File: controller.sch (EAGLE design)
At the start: 70 parts, among them J1 SATA0010225X, J10 ALED_A, J11 ALED_B, J12 ALED_C, J13 FRONT_PANEL, J14 12V, J15 5V, J16 3.3V, J2 USB, J3 ICSP, J4 PUMP, J5 FANS, J6 FLOW, J7 TEMP, J8 TACH_OUT, J9 SHUTDOWN, Q1 NMOSL, Q2 NMOSL, Q3 NMOSL, Q4 NMOSL, Q5 NMOSL, Q6 NMOSL, Q7 NMOSL, Q8 NMOSL, SW1 RESET, U1 PIC32MZ-EF-144, U2 NCP5501DT33, U3 MAX6071A_30, U4 TXU0104, U5 CPC1006N, Y1 24MHz

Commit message: Controller (hopefully) finished
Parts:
- added A1: VXO7805-500, BW-Active:VXO78-500
- added C23, C27: 0.1µF, rcl:C-EUC0603
- added C24: 22µF, rcl:C-EUC0603
- added C25: 10µF, rcl:C-EUC0805
- added C26: 100µF, rcl:CPOL-EUD
- added D1, D2: GS1A-L, BW-Active:DO-214AC-DIODE
- added J17: 12V_WD, pinhead:PINHD-1X2
- added K1: G5Q-1, BW-PassiveMechanical:G5Q-1
- added Q10, Q9: PMOS, BW-Active:SOT23-P-MOSFET
- added Q11: NMOSL, BW-Active:SOT23-N-MOSFET
- added R16, R18: 1kΩ, resistor:R-US_R0603
- added R17: 10kΩ, resistor:R-US_R0603
- added TP1, TP10, TP11, TP12, TP14, TP15, TP2, TP3, TP4, TP5, TP6, TP7, TP8, TP9: RCU-0(J), BW-PassiveMechanical:RCU-0(J)
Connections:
- new net 12V_PUMP: J4.2, K1G$2.P
- new net 12V_PUMP_WD: K1G$2.O, Q10.D
- new net 12V_WD: A1.IN, C25.1, C26.+, Q10.S, Q9.S, R17.2
- new net 12V_WD_PROTECT: Q9.G, R16.1
- new net 12V_WD_RAW: J17.1, Q9.D
- new net 5V_SB: C16.1, C19.1, D1.C, D2.C, J13.1, R12.1, R13.2, R7.2, R8.2, R9.2, TP5.TP, U2.IN, U3.EN, U3.IN
- new net 5V_WD: A1.OUT, C24.1, D2.A, R18.2
- new net PUMP_WD_DRIVE: Q10.G, Q11.D, R17.1
- new net PUMP_WD_RUN: Q11.G, U1.AN36/ETDX1/RJ9
- new net WD_DETECT: R18.1, U1.ERXD0/RH8
- net 12V: now also K1G$1.1, K1G$2.S; no longer J4.2
- net 3.3V: now also C27.1
- net 3V_REF: now also TP6.TP
- net 5V: no longer R12.1, R13.2
- net 5V_USB: now also C23.1, D1.A, TP4.TP; no longer C16.1, C19.1, J13.1, R7.2, R8.2, R9.2, U2.IN, U3.EN, U3.IN
- net ALED_A: now also TP1.TP
- net ALED_B: now also TP2.TP
- net ALED_C: now also TP3.TP
- net ALED_OE: now also TP15.TP
- net FAN_PWM: now also TP14.TP
- net FAN_TACH: now also TP12.TP
- net FLOW_TACH: now also TP8.TP
- net GND: now also A1.GND, C23.2, C24.2, C25.2, C26.-, C27.2, J17.2, K1G$1.2, Q11.S, R16.2
- net PUMP_PWM: now also TP11.TP
- net PUMP_TACH: now also TP10.TP
- net TACH_OUT: now also TP9.TP
- net TEMP_SENSE: now also TP7.TP
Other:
- moved on the sheet: C10, C11, C12, C4, C5, C6, C7, C8, C9, J4, J5, J8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

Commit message: Parts Ordered
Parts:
- R11: value 4.7kΩ -> 2kΩ
- U4: value TXU0104 -> TXU0304-3; device BW-Active:TXU0104 -> BW-Active:TXU0304-3
- U5: value CPC1006N -> CPC1017N; device BW-Active:CPC1006N -> BW-Active:CPC1017N
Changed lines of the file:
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@@
 <part name="C19" library="rcl" library_urn="urn:adsk.eagle:library:334" deviceset="C-EU" device="C0603" package3d_urn="urn:adsk.eagle:package:23616/2" value="0.1µF"/>
 <part name="C20" library="rcl" library_urn="urn:adsk.eagle:library:334" deviceset="C-EU" device="C0603" package3d_urn="urn:adsk.eagle:package:23616/2" value="0.1µF"/>
-<part name="U4" library="BW-Active" library_urn="urn:adsk.eagle:library:33783073" deviceset="TXU0104" device="" package3d_urn="urn:adsk.eagle:package:33783235/2"/>
+<part name="U4" library="BW-Active" library_urn="urn:adsk.eagle:library:33783073" deviceset="TXU0*04" device="-3" package3d_urn="urn:adsk.eagle:package:33783235/2" technology="3"/>
 <part name="R9" library="resistor" library_urn="urn:adsk.eagle:library:348" deviceset="R-US_" device="R0603" package3d_urn="urn:adsk.eagle:package:23555/3" value="100kΩ"/>
 <part name="R8" library="resistor" library_urn="urn:adsk.eagle:library:348" deviceset="R-US_" device="R0603" package3d_urn="urn:adsk.eagle:package:23555/3" value="100kΩ"/>
@@
 <part name="R10" library="resistor" library_urn="urn:adsk.eagle:library:348" deviceset="R-US_" device="R0603" package3d_urn="urn:adsk.eagle:package:23555/3" value="10kΩ"/>
 <part name="Q2" library="BW-Active" library_urn="urn:adsk.eagle:library:33783073" deviceset="SOT23-N-MOSFET" device="" package3d_urn="urn:adsk.eagle:package:33783194/2" value="NMOSL"/>
-<part name="U5" library="BW-Active" library_urn="urn:adsk.eagle:library:33783073" deviceset="CPC1006N" device="" package3d_urn="urn:adsk.eagle:package:33936582/2"/>
-<part name="R11" library="resistor" library_urn="urn:adsk.eagle:library:348" deviceset="R-US_" device="R0603" package3d_urn="urn:adsk.eagle:package:23555/3" value="4.7kΩ"/>
+<part name="U5" library="BW-Active" library_urn="urn:adsk.eagle:library:33783073" deviceset="CPC1017N" device="" package3d_urn="urn:adsk.eagle:package:33936582/3"/>
+<part name="R11" library="resistor" library_urn="urn:adsk.eagle:library:348" deviceset="R-US_" device="R0603" package3d_urn="urn:adsk.eagle:package:23555/3" value="2kΩ"/>
 <part name="Q3" library="BW-Active" library_urn="urn:adsk.eagle:library:33783073" deviceset="SOT23-N-MOSFET" device="" package3d_urn="urn:adsk.eagle:package:33783194/2" value="NMOSL"/>
 <part name="SJ1" library="jumper" library_urn="urn:adsk.eagle:library:252" deviceset="SJ" device="" package3d_urn="urn:adsk.eagle:package:15471/1" value="GNDLINK"/>
@@
 <wire x1="124.46" y1="124.46" x2="127" y2="124.46" width="0.1524" layer="91"/>
 <junction x="127" y="124.46"/>
-</segment>
-<segment>
+<wire x1="127" y1="124.46" x2="129.54" y2="124.46" width="0.1524" layer="91"/>
+<label x="129.54" y="124.46" size="1.778" layer="95"/>
+</segment>
+<segment>

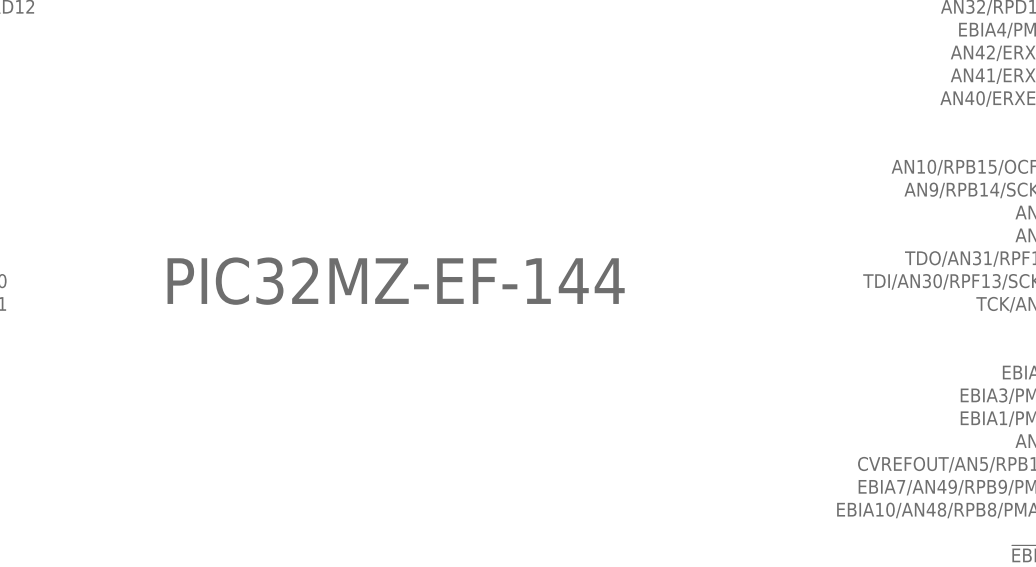
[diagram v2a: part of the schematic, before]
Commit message: Replaced MCU footprint due to earlier error
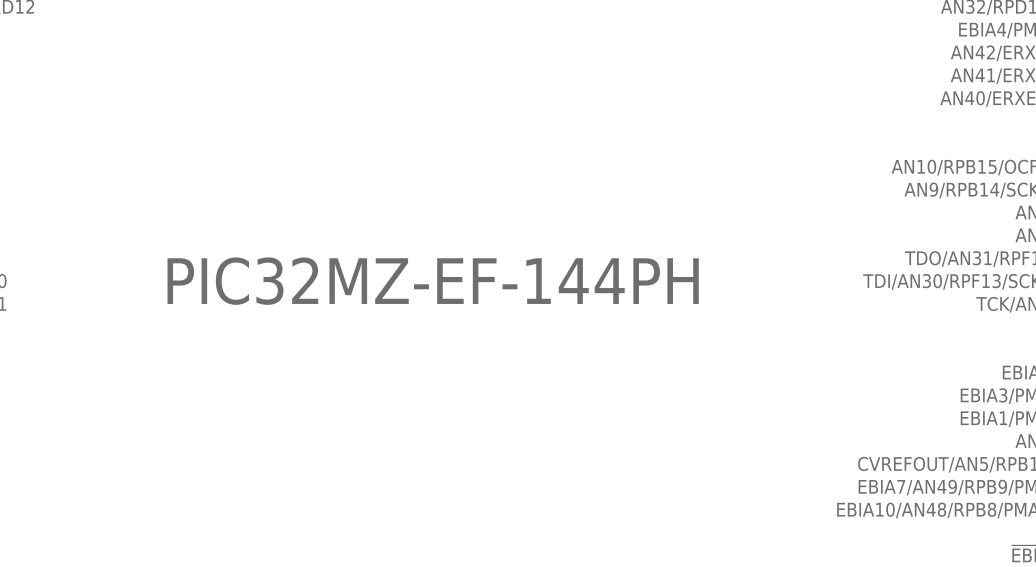
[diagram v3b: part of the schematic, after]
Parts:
- U1: value PIC32MZ-EF-144 -> PIC32MZ-EF-144PH; device BW-Active:PIC32MZ-EF-144 -> BW-Active:PIC32MZ-EF-144PH
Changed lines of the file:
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@@
 </classes>
 <parts>
-<part name="U1" library="BW-Active" library_urn="urn:adsk.eagle:library:33783073" deviceset="PIC32MZ-EF-144" device="" package3d_urn="urn:adsk.eagle:package:33783198/2"/>
+<part name="U1" library="BW-Active" library_urn="urn:adsk.eagle:library:33783073" deviceset="PIC32MZ-EF-144" device="PH" package3d_urn="urn:adsk.eagle:package:34569132/2" value="PIC32MZ-EF-144PH"/>
 <part name="J4" library="BW-Connectors" library_urn="urn:adsk.eagle:library:33858393" deviceset="47053-1000" device="" package3d_urn="urn:adsk.eagle:package:33998595/2" value="PUMP"/>
 <part name="J5" library="BW-Connectors" library_urn="urn:adsk.eagle:library:33858393" deviceset="47053-1000" device="" package3d_urn="urn:adsk.eagle:package:33998595/2" value="FANS"/>
@@
 <part name="J2" library="pinhead" library_urn="urn:adsk.eagle:library:325" deviceset="PINHD-1X4" device="" package3d_urn="urn:adsk.eagle:package:22407/2" value="USB"/>
 <part name="J3" library="BW-Connectors" library_urn="urn:adsk.eagle:library:33858393" deviceset="5PIN-1.27" device="" package3d_urn="urn:adsk.eagle:package:33858429/2" value="ICSP"/>
-<part name="J1" library="BW-Connectors" library_urn="urn:adsk.eagle:library:33858393" deviceset="SATA0010225X" device="" package3d_urn="urn:adsk.eagle:package:33985671/4"/>
+<part name="J1" library="BW-Connectors" library_urn="urn:adsk.eagle:library:33858393" deviceset="SATA0010225X" device="" package3d_urn="urn:adsk.eagle:package:33985671/5"/>
 <part name="LS1" library="BW-Active" library_urn="urn:adsk.eagle:library:33783073" deviceset="AI-1224-TWT-5V-R" device="" package3d_urn="urn:adsk.eagle:package:33999453/3"/>
 <part name="Y1" library="BW-PassiveMechanical" library_urn="urn:adsk.eagle:library:33858467" deviceset="HC49/4HSMX-CRYSTAL" device="" package3d_urn="urn:adsk.eagle:package:34006902/2" value="24MHz"/>
